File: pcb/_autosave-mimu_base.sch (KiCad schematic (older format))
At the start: 16 parts, among them J1 OPT, SW2 SW_DPDT_x2, U1 AQY211EH, U2 ATTINY88AU

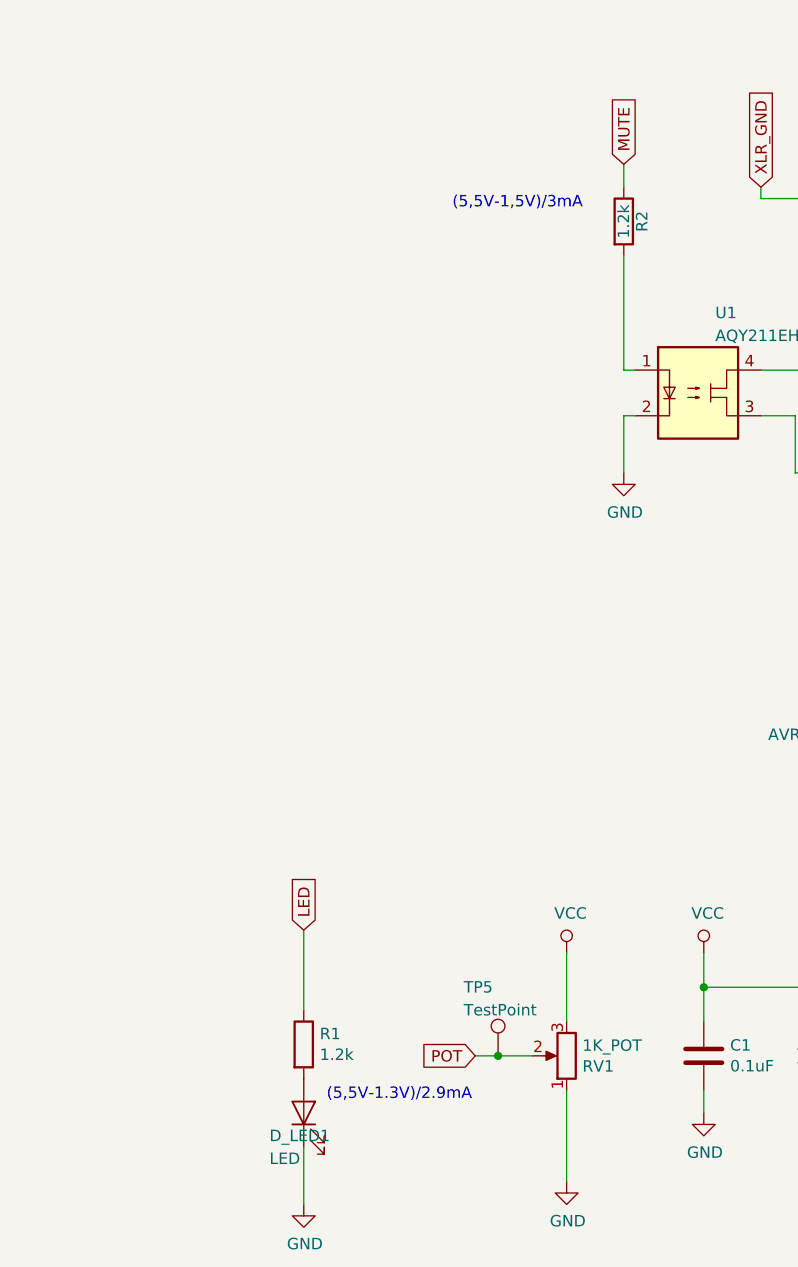
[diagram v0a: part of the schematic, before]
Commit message: Resistor Values now Reality-proven
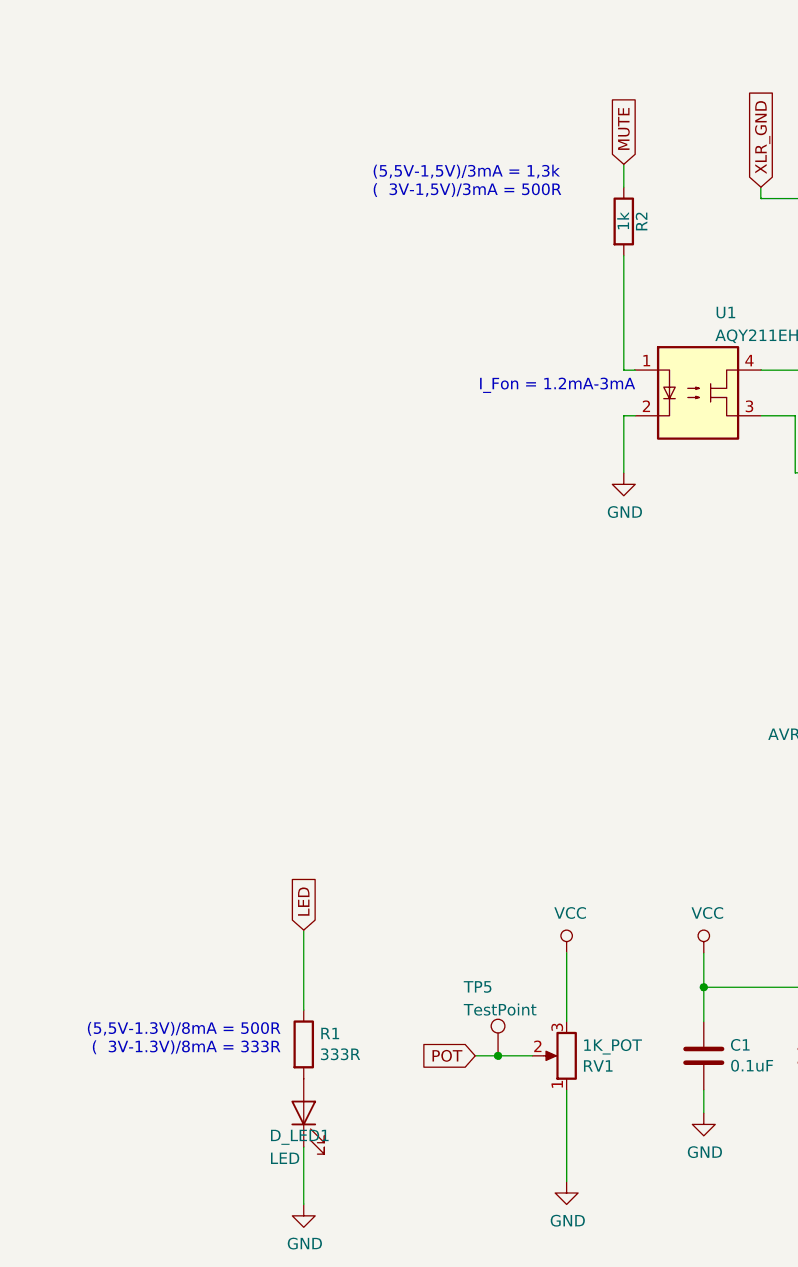
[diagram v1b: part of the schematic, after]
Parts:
- R1: value 1.2k -> 333R
- R2: value 1.2k -> 1k
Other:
- note added: "(5,5V-1,5V)/3mA = 1,3k\n( 3V-1,5V)/3mA = 500R"
- note added: "(5,5V-1.3V)/8mA = 500R\n( 3V-1.3V)/8mA = 333R"
- note added: "I_Fon = 1.2mA-3mA"
- note removed: "(5,5V-1,5V)/3mA"
- note removed: "(5,5V-1.3V)/2.9mA"
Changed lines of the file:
@@
 P 2550 5550
 F 0 "R1" H 2620 5596 50  0000 L CNN
-F 1 "1.2k" H 2620 5505 50  0000 L CNN
+F 1 "333R" H 2620 5505 50  0000 L CNN
 F 2 "Resistor_SMD:R_1206_3216Metric_Pad1.42x1.75mm_HandSolder" V 2480 5550 50  0001 C CNN
 F 3 "~" H 2550 5550 50  0001 C CNN
@@
 P 3950 1950
 F 0 "R2" V 4030 1950 50  0000 C CNN
-F 1 "1.2k" V 3950 1950 50  0000 C CNN
+F 1 "1k" V 3950 1950 50  0000 C CNN
 F 2 "Resistor_SMD:R_1206_3216Metric_Pad1.42x1.75mm_HandSolder" V 3880 1950 50  0001 C CNN
 F 3 "" H 3950 1950 50  0001 C CNN
@@
 Wire Wire Line
 	3400 5600 3300 5600
-Text Notes 2650 5800 0    50   ~ 0
-(5,5V-1.3V)/2.9mA
-Text Notes 3200 1900 0    50   ~ 0
-(5,5V-1,5V)/3mA
+Text Notes 2450 5600 2    50   ~ 0
+(5,5V-1.3V)/8mA = 500R\n(  3V-1.3V)/8mA = 333R
+Text Notes 2850 1850 0    50   ~ 0
+(5,5V-1,5V)/3mA = 1,3k\n(  3V-1,5V)/3mA = 500R
+Text Notes 4000 2700 2    50   ~ 0
+I_Fon = 1.2mA-3mA
 $EndSCHEMATC
